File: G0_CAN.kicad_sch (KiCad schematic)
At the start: 31 parts, among them J1 USB_C_Receptacle_USB2.0, J12 CAN1, J13 CAN2, U1 Nucleo-64-G0B1, U2 TJA1051TK-3, U3 TJA1051TK-3

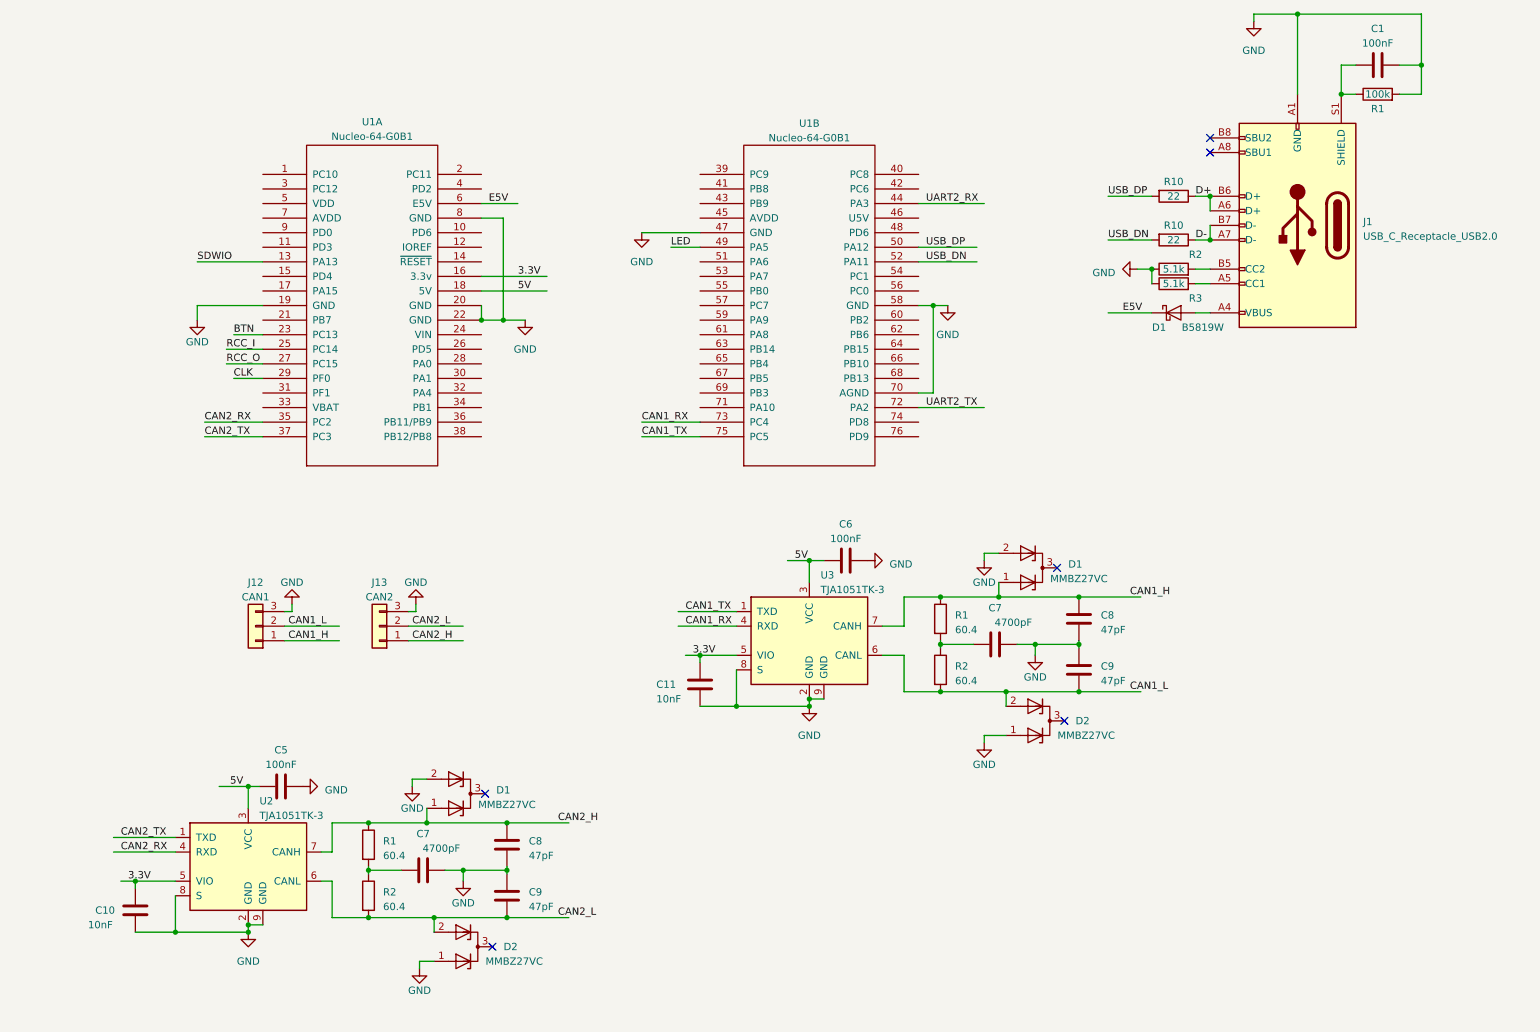
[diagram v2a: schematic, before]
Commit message: Make the G0-CAN board use isolated CAN.
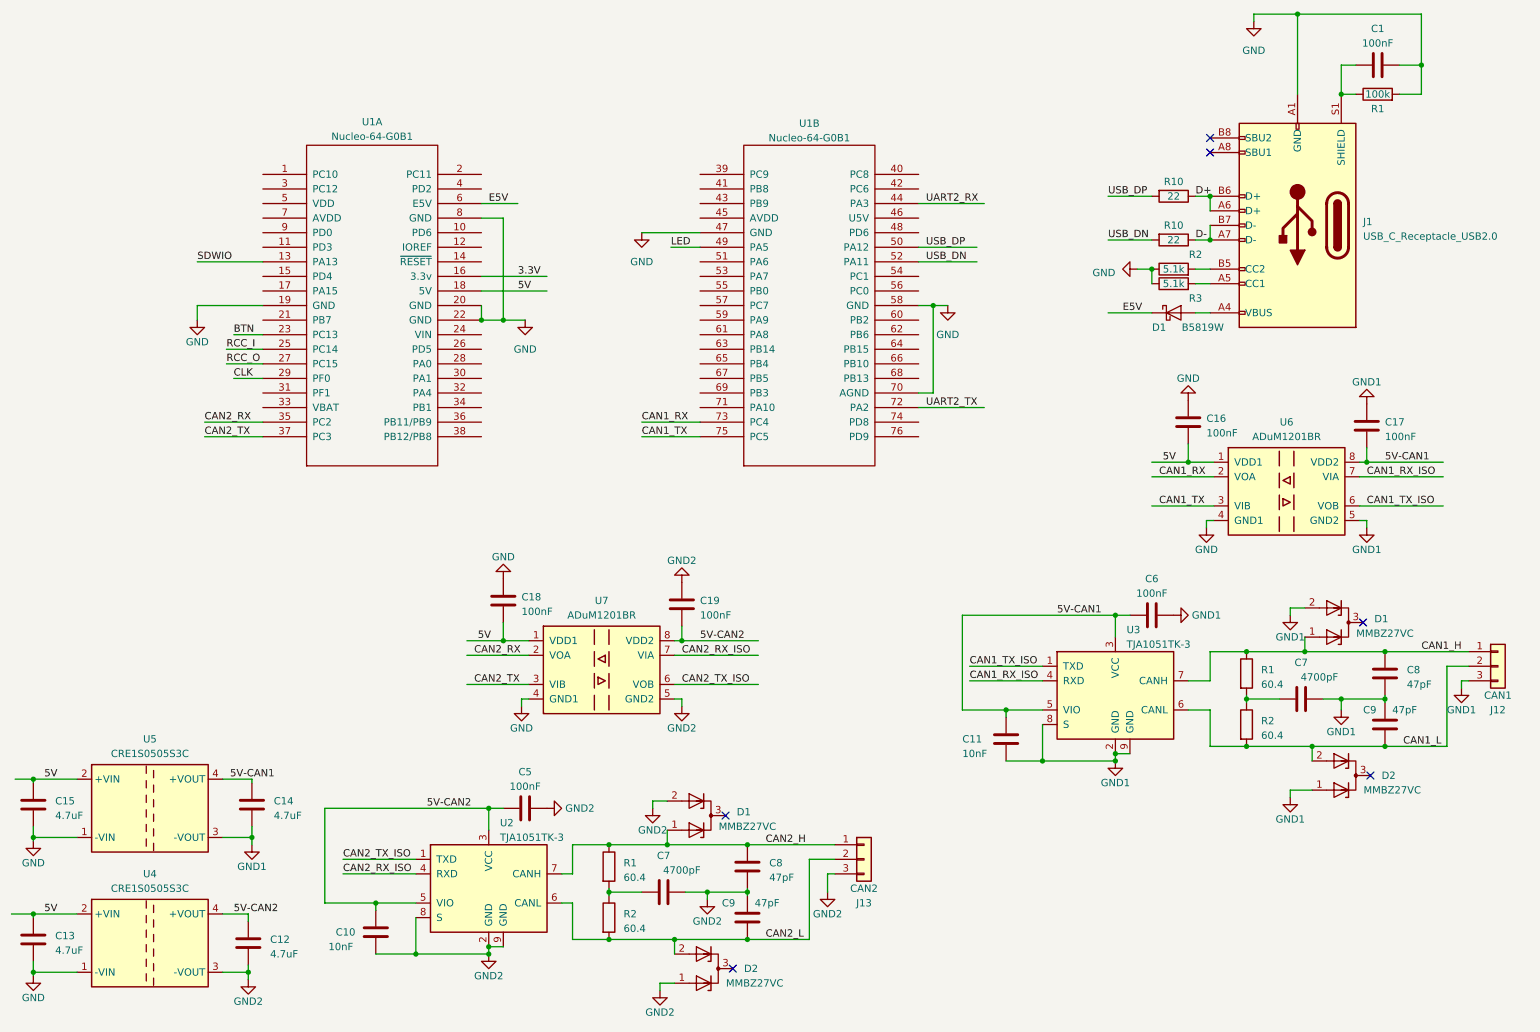
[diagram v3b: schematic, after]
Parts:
- added C12, C13, C14, C15: 4.7uF, Capacitor_SMD:C_0805_2012Metric, symbol Device:C
- added C16, C17, C18, C19: 100nF, Capacitor_SMD:C_0603_1608Metric, symbol Device:C
- added U4, U5: CRE1S0505S3C, Converter_DCDC:Converter_DCDC_Murata_CRE1xxxxxx3C_THT, symbol Regulator_Switching:CRE1S0505S3C
- added U6, U7: ADuM1201BR, Package_SO:SOIC-8_3.9x4.9mm_P1.27mm, symbol Isolator:ADuM1201BR
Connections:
- net 3.3V: no longer C10.2, C11.2, U2.5 (VIO), U3.5 (VIO)
- net 5V: now also C13.1, C15.1, C16.1, C18.1, U4.2 (+VIN), U5.2 (+VIN), U6.1 (VDD1), U7.1 (VDD1); no longer C5.1, C6.1, U2.3 (VCC), U3.3 (VCC)
- net CAN1_RX: now also U6.2 (VOA); no longer U3.4 (RXD)
- net CAN1_TX: now also U6.3 (VIB); no longer U3.1 (TXD)
- net CAN2_RX: now also U7.2 (VOA); no longer U2.4 (RXD)
- net CAN2_TX: now also U7.3 (VIB); no longer U2.1 (TXD)
- net GND: now also C13.2, C15.2, C16.2, C18.2, U4.1 (-VIN), U5.1 (-VIN), U6.4 (GND1), U7.4 (GND1); no longer C10.1, C11.1, C5.2, C6.2, C7.2, C7.2, C8.2, C8.2, C9.1, C9.1, D1.2 (K), D1.2 (K), D2.1 (K), D2.1 (K), J12.3 (Pin_3), J13.3 (Pin_3), U2.2 (GND), U2.8 (S), U2.9 (GND), U3.2 (GND), U3.8 (S), U3.9 (GND)
- new net 5V-CAN1: C11.2, C14.1, C17.1, C6.1, U3.3 (VCC), U3.5 (VIO), U5.4 (+VOUT), U6.8 (VDD2)
- new net 5V-CAN2: C10.2, C12.1, C19.1, C5.1, U2.3 (VCC), U2.5 (VIO), U4.4 (+VOUT), U7.8 (VDD2)
- new net CAN1_RX_ISO: U3.4 (RXD), U6.7 (VIA)
- new net CAN1_TX_ISO: U3.1 (TXD), U6.6 (VOB)
- new net CAN2_RX_ISO: U2.4 (RXD), U7.7 (VIA)
- new net CAN2_TX_ISO: U2.1 (TXD), U7.6 (VOB)
- new net GND1: C11.1, C14.2, C17.2, C6.2, C7.2, C8.2, C9.1, D1.2 (K), D2.1 (K), J12.3 (Pin_3), U3.2 (GND), U3.8 (S), U3.9 (GND), U5.3 (-VOUT), U6.5 (GND2)
- new net GND2: C10.1, C12.2, C19.2, C5.2, C7.2, C8.2, C9.1, D1.2 (K), D2.1 (K), J13.3 (Pin_3), U2.2 (GND), U2.8 (S), U2.9 (GND), U4.3 (-VOUT), U7.5 (GND2)
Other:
- moved on the sheet: C10, C11, C5, C6, C7, C8, C9, D1, D2, J12, J13, R1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

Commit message: Flip the nucleo connector.
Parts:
- U6, U7: value ADuM1201BR -> NSi8121N0; LCSC Part # C87626 -> C399510; Part # (none) -> NSi8121Nx or Si8621xx(pins may vary)
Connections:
- net CAN1_RX: now also U1.35 (PC2); no longer U1.73 (PC4)
- net CAN1_TX: now also U1.37 (PC3); no longer U1.75 (PC5)
- net CAN2_RX: now also U1.73 (PC4); no longer U1.35 (PC2)
- net CAN2_TX: now also U1.75 (PC5); no longer U1.37 (PC3)
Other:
- note added: "Note CAN1_XX and CAN2_XX labels are swapped CAN1_XX are connected to FDCAN2 and CAN2_XX are connected to FDCAN1"
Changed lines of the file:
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@@
     (stroke (width 0) (type default))
   )
+  (text "Note CAN1_XX and CAN2_XX labels are swapped\nCAN1_XX are connected to FDCAN2 and\nCAN2_XX are connected to FDCAN1"
+    (at 20.955 103.505 0)
+    (effects (font (size 1.27 1.27)) (justify left bottom))
+  )
   (label "CAN2_TX_ISO" (at 135.255 138.43 0) (fields_autoplaced)
     (effects (font (size 1.27 1.27)) (justify left bottom))
@@
     (effects (font (size 1.27 1.27)) (justify left bottom))
   )
-  (label "CAN2_TX" (at 52.07 95.25 0) (fields_autoplaced)
+  (label "CAN2_TX" (at 128.905 95.25 0) (fields_autoplaced)
     (effects (font (size 1.27 1.27)) (justify left bottom))
   )
@@
     (effects (font (size 1.27 1.27)) (justify left bottom))
   )
-  (label "CAN1_TX" (at 128.27 95.25 0) (fields_autoplaced)
+  (label "CAN1_TX" (at 52.705 95.25 0) (fields_autoplaced)
     (effects (font (size 1.27 1.27)) (justify left bottom))
   )
@@
     (effects (font (size 1.27 1.27)) (justify left bottom))
   )
-  (label "CAN2_RX" (at 52.07 92.71 0) (fields_autoplaced)
+  (label "CAN2_RX" (at 128.905 92.71 0) (fields_autoplaced)
     (effects (font (size 1.27 1.27)) (justify left bottom))
   )
@@
     (effects (font (size 1.27 1.27)) (justify left bottom))
   )
-  (label "CAN1_RX" (at 128.27 92.71 0) (fields_autoplaced)
+  (label "CAN1_RX" (at 52.705 92.71 0) (fields_autoplaced)
     (effects (font (size 1.27 1.27)) (justify left bottom))
   )
@@
   (symbol (lib_id "Isolator:ADuM1201BR") (at 121.285 135.89 0) (unit 1)
     (in_bom yes) (on_board yes) (dnp no) (fields_autoplaced)
-    (property "Reference" "U7" (at 121.285 123.825 0)
-      (effects (font (size 1.27 1.27)))
-    )
-    (property "Value" "ADuM1201BR" (at 121.285 126.365 0)
+    (property "Reference" "U7" (at 121.285 124.46 0)
+      (effects (font (size 1.27 1.27)))
+    )
+    (property "Value" "NSi8121N0" (at 121.285 127 0)
       (effects (font (size 1.27 1.27)))
     )
@@
       (effects (font (size 1.27 1.27)) hide)
     )
-    (property "LCSC Part #" "C87626" (at 121.285 135.89 0)
+    (property "LCSC Part #" "C399510" (at 121.285 135.89 0)
+      (effects (font (size 1.27 1.27)) hide)
+    )
+    (property "Part #" "NSi8121Nx or Si8621xx(pins may vary)" (at 121.285 135.89 0)
       (effects (font (size 1.27 1.27)) hide)
     )
@@
       (effects (font (size 1.27 1.27)))
     )
-    (property "Value" "ADuM1201BR" (at 240.665 95.25 0)
+    (property "Value" "NSi8121N0" (at 240.665 95.25 0)
       (effects (font (size 1.27 1.27)))
     )
@@
       (effects (font (size 1.27 1.27)) hide)
     )
-    (property "LCSC Part #" "C87626" (at 240.665 104.775 0)
-      (effects (font (size 1.27 1.27)) hide)
-    )
+    (property "LCSC Part #" "C399510" (at 240.665 104.775 0)
+      (effects (font (size 1.27 1.27)) hide)
+    )
+    (property "Part #" "NSi8121Nx or Si8621xx(pins may vary)" (at 240.665 104.775 0)
+      (effects (font (size 1.27 1.27)) hide)
+    )

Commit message: Add TX/RX leds to the CAN shield.
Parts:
- added D6, D7: TX, LED_SMD:LED_0603_1608Metric, symbol Device:LED
- added D8, D9: RX, LED_SMD:LED_0603_1608Metric, symbol Device:LED
- added R10 (x4): 22, Resistor_SMD:R_0603_1608Metric, symbol Device:R
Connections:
- net 3.3V: now also R10.1, R10.1, R10.1, R10.1
- net CAN2_TX_LED: now reaches U1.65 (PB4)
- net CAN2_TX_LED: now also D7.1 (K)
- net CAN2_RX_LED: now reaches U1.67 (PB5)
- net CAN2_RX_LED: now also D9.1 (K)
- net CAN1_TX_LED: now reaches U1.28 (PA0)
- net CAN1_TX_LED: now also D6.1 (K)
- net CAN1_RX_LED: now reaches U1.30 (PA1)
- net CAN1_RX_LED: now also D8.1 (K)
- new net: D6.2 (A), R10.2
- new net: D9.2 (A), R10.2
- new net: D7.2 (A), R10.2
- new net: D8.2 (A), R10.2

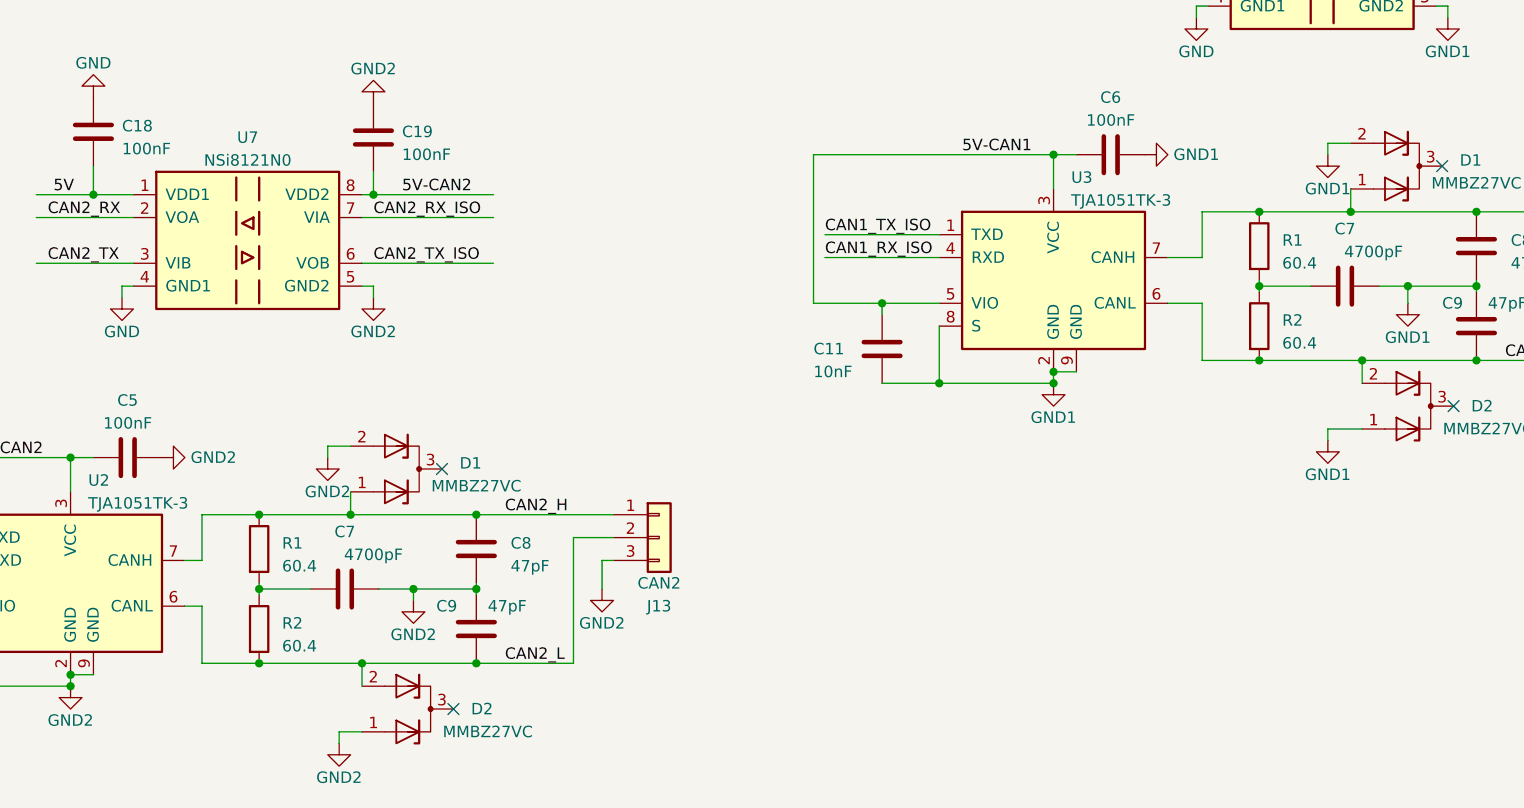
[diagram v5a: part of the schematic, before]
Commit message: Add terminator jumpers.
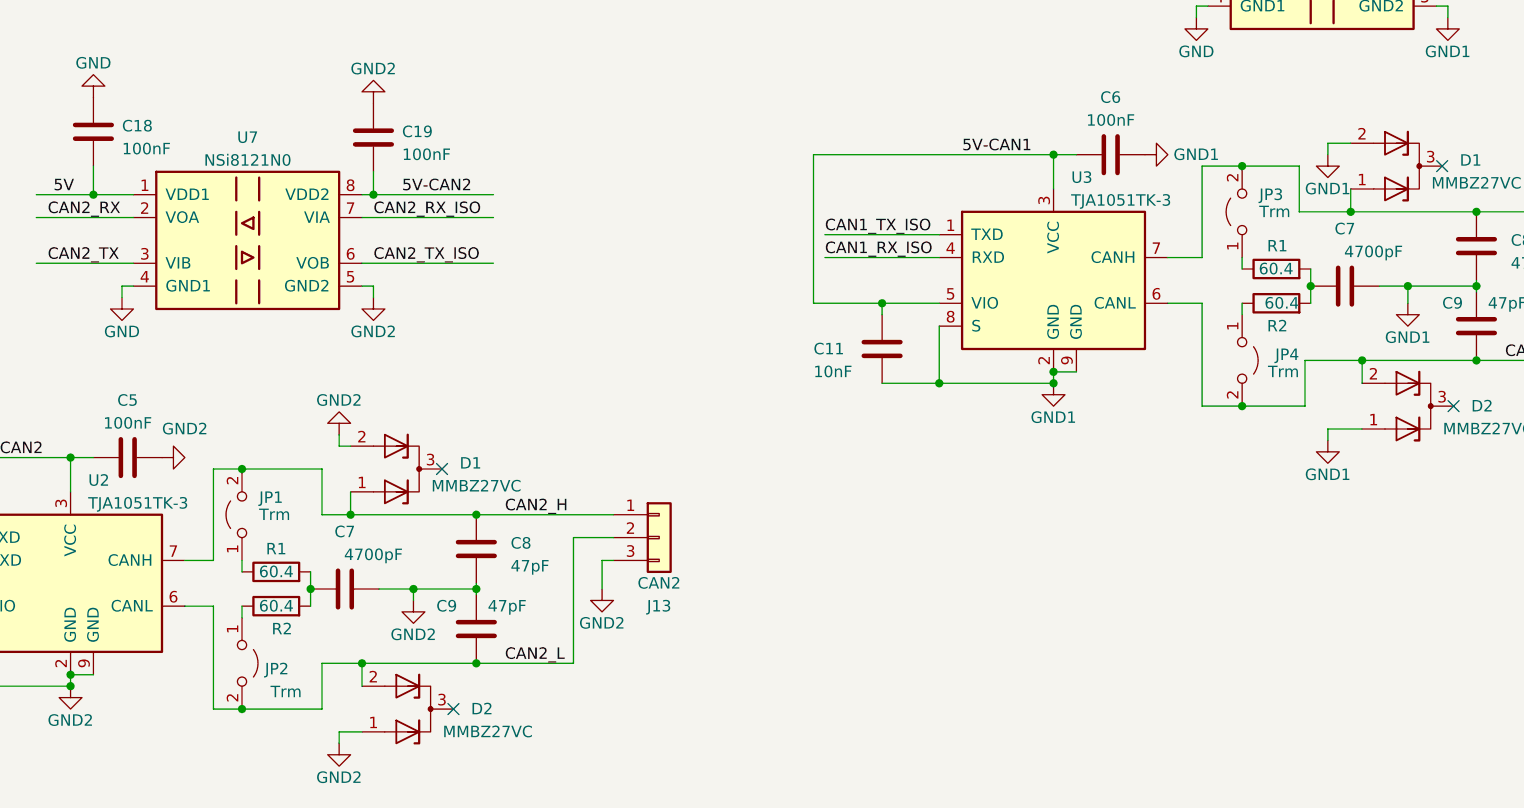
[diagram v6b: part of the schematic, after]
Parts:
- added JP1, JP2, JP3, JP4: Trm, Connector_PinHeader_2.00mm:PinHeader_1x02_P2.00mm_Vertical, symbol Jumper:Jumper_2_Open
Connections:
- net CAN1_H: now also JP3.2 (B); no longer R1.1
- net CAN1_L: now also JP4.2 (B); no longer R2.2
- net CAN2_H: now also JP1.2 (B); no longer R1.1
- net CAN2_L: now also JP2.2 (B); no longer R2.2
- net at C7.1, R1.2: now also R2.2; no longer R2.1 (x2)
- new net: JP3.1 (A), R1.1
- new net: JP1.1 (A), R1.1
- new net: JP2.1 (A), R2.1
- new net: JP4.1 (A), R2.1
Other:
- moved on the sheet: R1, R2
